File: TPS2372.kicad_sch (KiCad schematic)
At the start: 53 parts

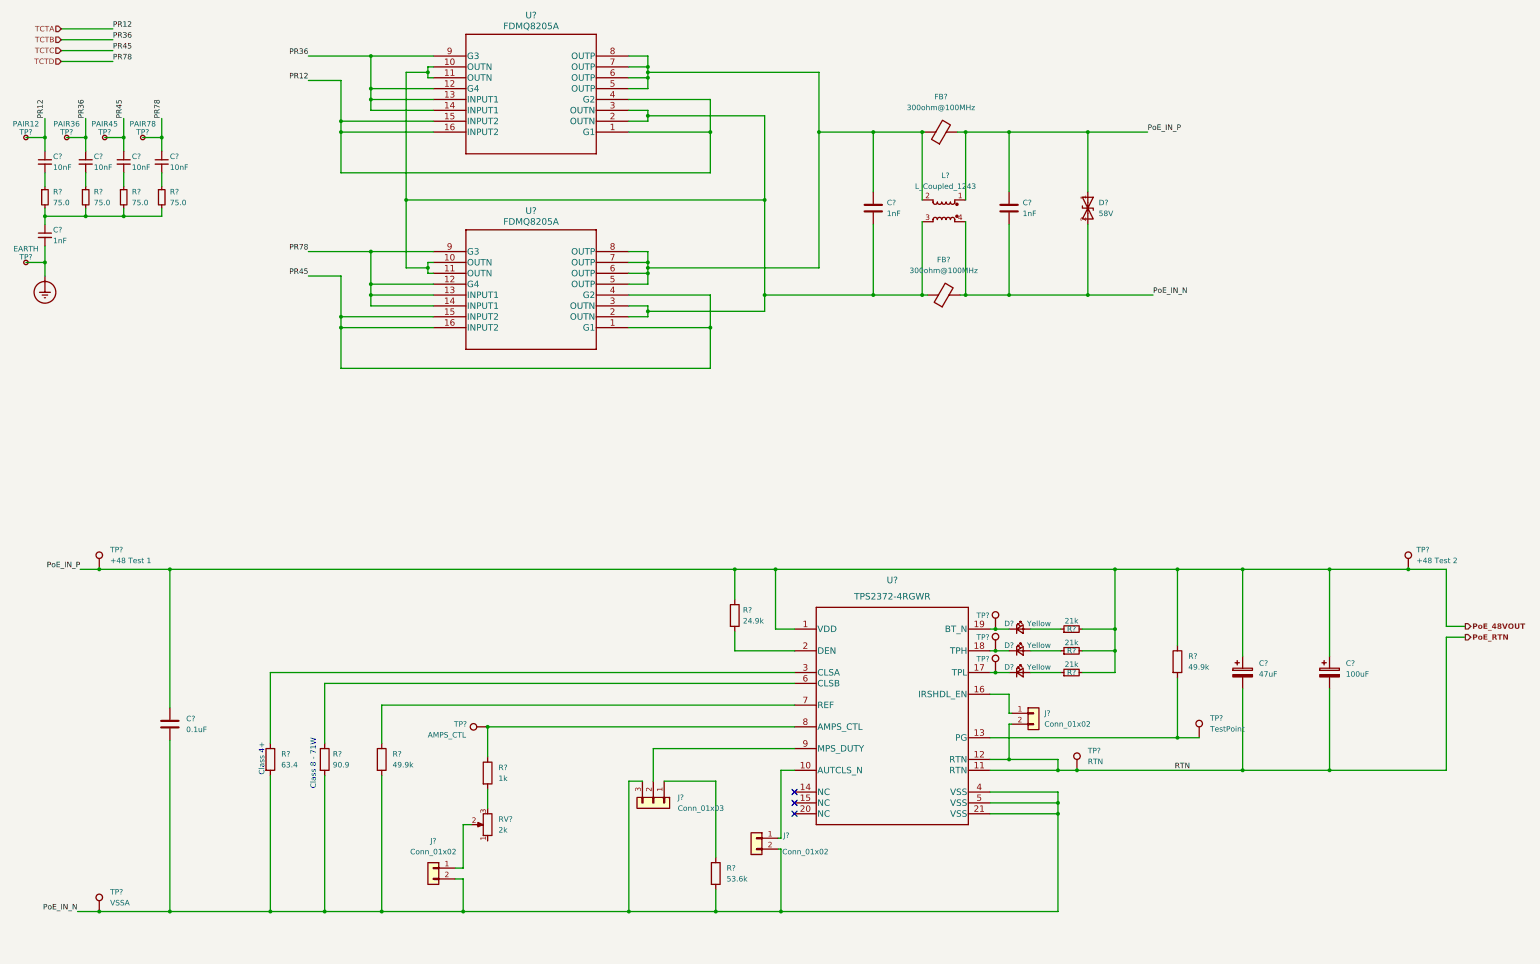
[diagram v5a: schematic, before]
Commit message: finished lm5116 circuit foot print assignment
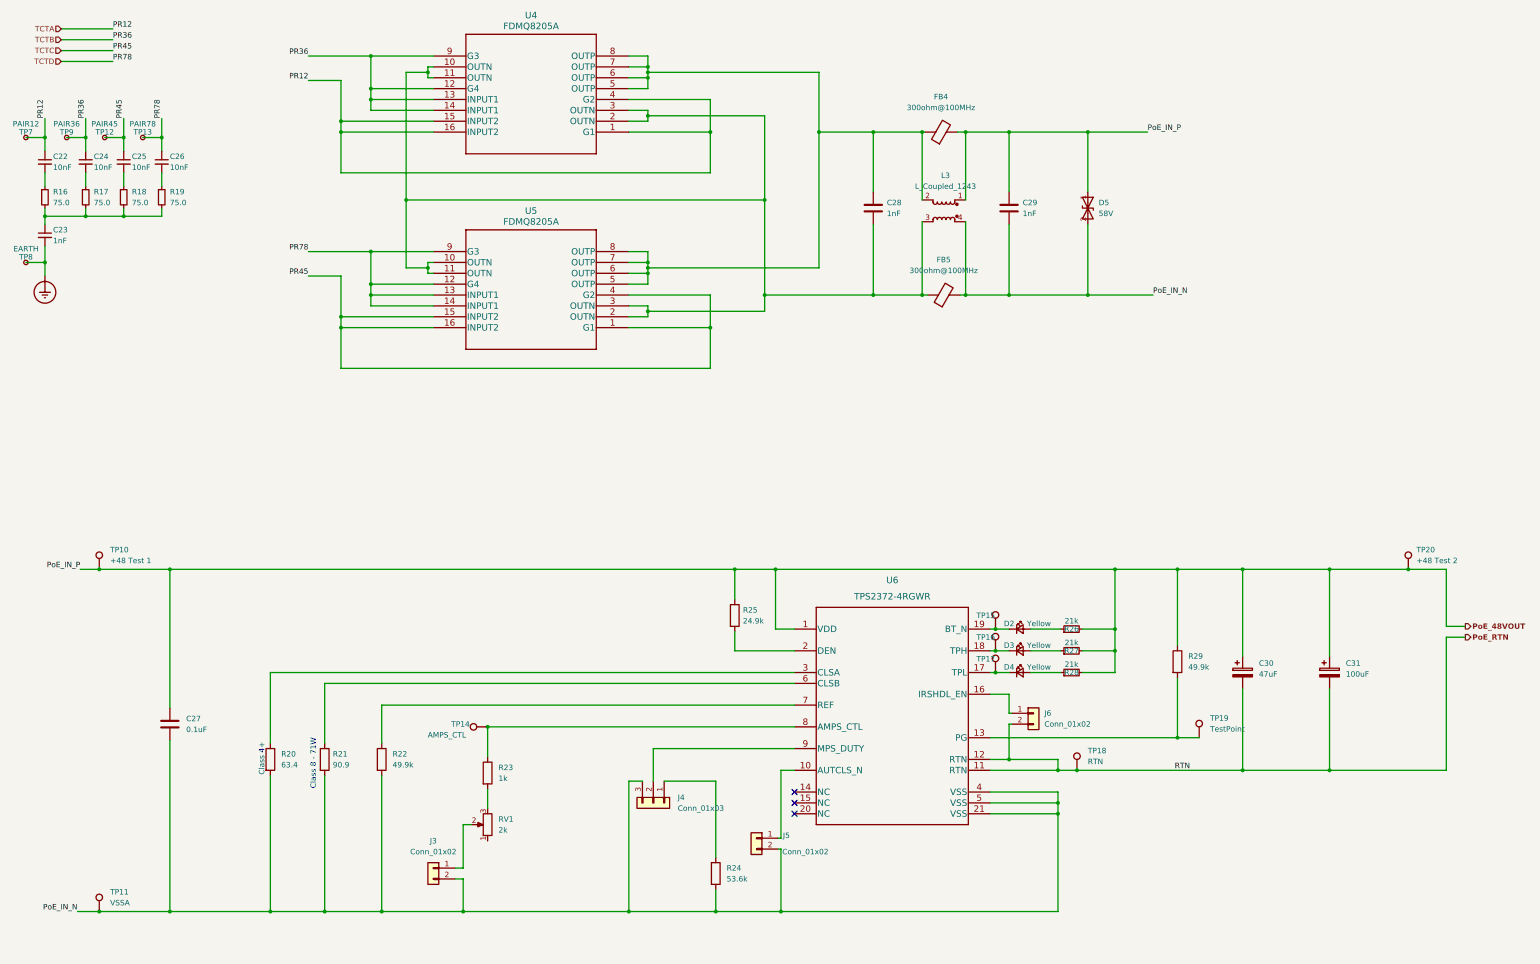
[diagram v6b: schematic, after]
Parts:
- gave numbers to parts that had none: 53

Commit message: Footprint done
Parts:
- removed J3, J5: Conn_01x02, TestPoint:TestPoint_2Pads_Pitch2.54mm_Drill0.8mm, symbol Connector_Generic:Conn_01x02
- removed J4: Conn_01x03, symbol Connector_Generic:Conn_01x03
- removed R24: 53.6k, symbol Device:R
- removed RV1: 2k, symbol Device:R_Potentiometer
- removed TP14: AMPS_CTL, symbol Connector:TestPoint
- C22, C23, C24, C25, C26, C28, C29: footprint (none) -> Capacitor_SMD:C_0603_1608Metric
- C27: footprint (none) -> Capacitor_SMD:C_0805_2012Metric
- C30: footprint (none) -> PoE_Devices:EEV-TG2A470Q
- C31: footprint (none) -> Capacitor_SMD:CP_Elec_16x17.5
- D2, D3, D4: footprint (none) -> Diode_SMD:D_0603_1608Metric
- D5: footprint (none) -> Diode_SMD:D_SMB
- FB4, FB5: footprint (none) -> Inductor_SMD:L_0603_1608Metric
- J6: footprint TestPoint:TestPoint_2Pads_Pitch2.54mm_Drill0.8mm -> Connector_PinHeader_2.54mm:PinHeader_1x02_P2.54mm_Vertical
- L3: footprint (none) -> PoE_Devices:744272251
- R16, R17, R18, R19, R21, R22, R25, R26, R27, R28, R29: footprint (none) -> Resistor_SMD:R_0603_1608Metric
- R20: footprint (none) -> Resistor_SMD:R_0201_0603Metric
- R23: value 1k -> 0; footprint (none) -> Resistor_SMD:R_0603_1608Metric
- U4, U5: footprint MLP_4p5X5_ONS -> PoE_Devices:FDMQ8205A
- U6: footprint RGW0020B -> PoE_Devices:TPS2372-3RGWR
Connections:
- net PoE_IN_N: now also R23.2
- net at U6.8 (AMPS_CTL): no longer R23.1
- net at U6.9 (MPS_DUTY): now also R23.1
- no-connect marks 3 -> 5
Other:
- note added: "Must Support At Least 60Volts"
- note added: "Near MOS Input"
- moved on the sheet: C23, R23

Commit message: Update PCB
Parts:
- TP10, TP11, TP12, TP13, TP15, TP16, TP17, TP18, TP19, TP20, TP7, TP8, TP9: footprint (none) -> TestPoint:TestPoint_Pad_1.0x1.0mm
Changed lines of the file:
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@@
     (property "Reference" "TP12" (id 0) (at 35.56 45.085 90))
     (property "Value" "PAIR45" (id 1) (at 35.56 43.18 90))
-    (property "Footprint" "" (id 2) (at 35.56 41.275 0)
+    (property "Footprint" "TestPoint:TestPoint_Pad_1.0x1.0mm" (id 2) (at 35.56 41.275 0)
       (effects (font (size 1.27 1.27)) hide)
     )
@@
       (effects (font (size 1.27 1.27)) (justify left))
     )
-    (property "Footprint" "" (id 2) (at 39.37 227.33 0)
+    (property "Footprint" "TestPoint:TestPoint_Pad_1.0x1.0mm" (id 2) (at 39.37 227.33 0)
       (effects (font (size 1.27 1.27)) hide)
     )
@@
       (effects (font (size 1.27 1.27)) (justify left))
     )
-    (property "Footprint" "" (id 2) (at 345.44 147.32 0)
+    (property "Footprint" "TestPoint:TestPoint_Pad_1.0x1.0mm" (id 2) (at 345.44 147.32 0)
       (effects (font (size 1.27 1.27)) hide)
     )
@@
     (property "Reference" "TP9" (id 0) (at 26.67 45.085 90))
     (property "Value" "PAIR36" (id 1) (at 26.67 43.18 90))
-    (property "Footprint" "" (id 2) (at 26.67 41.275 0)
+    (property "Footprint" "TestPoint:TestPoint_Pad_1.0x1.0mm" (id 2) (at 26.67 41.275 0)
       (effects (font (size 1.27 1.27)) hide)
     )
@@
     (property "Reference" "TP7" (id 0) (at 17.145 45.085 90))
     (property "Value" "PAIR12" (id 1) (at 17.145 43.18 90))
-    (property "Footprint" "" (id 2) (at 17.145 41.275 0)
+    (property "Footprint" "TestPoint:TestPoint_Pad_1.0x1.0mm" (id 2) (at 17.145 41.275 0)
       (effects (font (size 1.27 1.27)) hide)
     )
@@
       (effects (font (size 1.27 1.27)) (justify left) hide)
     )
-    (property "Footprint" "" (id 2) (at 248.92 166.37 0)
+    (property "Footprint" "TestPoint:TestPoint_Pad_1.0x1.0mm" (id 2) (at 248.92 166.37 0)
       (effects (font (size 1.27 1.27)) hide)
     )
@@
       (effects (font (size 1.27 1.27)) (justify left))
     )
-    (property "Footprint" "" (id 2) (at 267.97 194.31 0)
+    (property "Footprint" "TestPoint:TestPoint_Pad_1.0x1.0mm" (id 2) (at 267.97 194.31 0)
       (effects (font (size 1.27 1.27)) hide)
     )
@@
     (property "Reference" "TP13" (id 0) (at 44.45 45.085 90))
     (property "Value" "PAIR78" (id 1) (at 44.45 43.18 90))
-    (property "Footprint" "" (id 2) (at 44.45 41.275 0)
+    (property "Footprint" "TestPoint:TestPoint_Pad_1.0x1.0mm" (id 2) (at 44.45 41.275 0)
       (effects (font (size 1.27 1.27)) hide)
     )
@@
     (property "Reference" "TP8" (id 0) (at 17.145 74.295 90))
     (property "Value" "EARTH" (id 1) (at 17.145 72.39 90))
-    (property "Footprint" "" (id 2) (at 17.145 70.485 0)
+    (property "Footprint" "TestPoint:TestPoint_Pad_1.0x1.0mm" (id 2) (at 17.145 70.485 0)
       (effects (font (size 1.27 1.27)) hide)
     )
@@
       (effects (font (size 1.27 1.27)) (justify left) hide)
     )
-    (property "Footprint" "" (id 2) (at 248.92 171.45 0)
+    (property "Footprint" "TestPoint:TestPoint_Pad_1.0x1.0mm" (id 2) (at 248.92 171.45 0)
       (effects (font (size 1.27 1.27)) hide)
     )
@@
       (effects (font (size 1.27 1.27)) (justify left))
     )
-    (property "Footprint" "" (id 2) (at 296.545 186.69 0)
+    (property "Footprint" "TestPoint:TestPoint_Pad_1.0x1.0mm" (id 2) (at 296.545 186.69 0)
       (effects (font (size 1.27 1.27)) hide)
     )
@@
       (effects (font (size 1.27 1.27)) (justify left) hide)
     )
-    (property "Footprint" "" (id 2) (at 248.92 161.29 0)
+    (property "Footprint" "TestPoint:TestPoint_Pad_1.0x1.0mm" (id 2) (at 248.92 161.29 0)
       (effects (font (size 1.27 1.27)) hide)
     )
@@
       (effects (font (size 1.27 1.27)) (justify left))
     )
-    (property "Footprint" "" (id 2) (at 39.37 147.32 0)
-      (effects (font (size 1.27 1.27)) hide)
-    )
+    (property "Footprint" "TestPoint:TestPoint_Pad_1.0x1.0mm" (id 2) (at 39.37 147.32 0)
+      (effects (font (size 1.27 1.27)) hide)
+    )
